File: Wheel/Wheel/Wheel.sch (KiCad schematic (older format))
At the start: 129 parts, among them J1 Conn_02x09_Odd_Even, J10 RJ45, J11 Screw_Terminal_01x02, J12 DS-201, J13 Conn_01x04, J14 Conn_02x13_Top_Bottom, J15 DB25_Female, J16 Conn_01x06, J17 Conn_01x07, J18 Conn_01x06, J19 RJ45, J2 RJ45, J20 DB9_Male, J21 DB9_Female, J22 Conn_02x15_Odd_Even, J3 RJ45, J4 RJ45, J5 USB_B, J6 Conn_02x10_Odd_Even, J7 Conn_02x09_Odd_Even, J8 RJ45, J9 RJ45, U1 MCP23S17_SP, U10 PC817, U11 IP4220CZ6, U12 PC817, U13 IP4220CZ6, U2 STM32F407VETx, U3 MCP23S17_SP, U4 USBLC6-2SC6, U5 AMS1117, U6 4N35, U7 PC817, U8 PC817, U9 PC817, Y1 32,768 кГц, Y2 8MHz

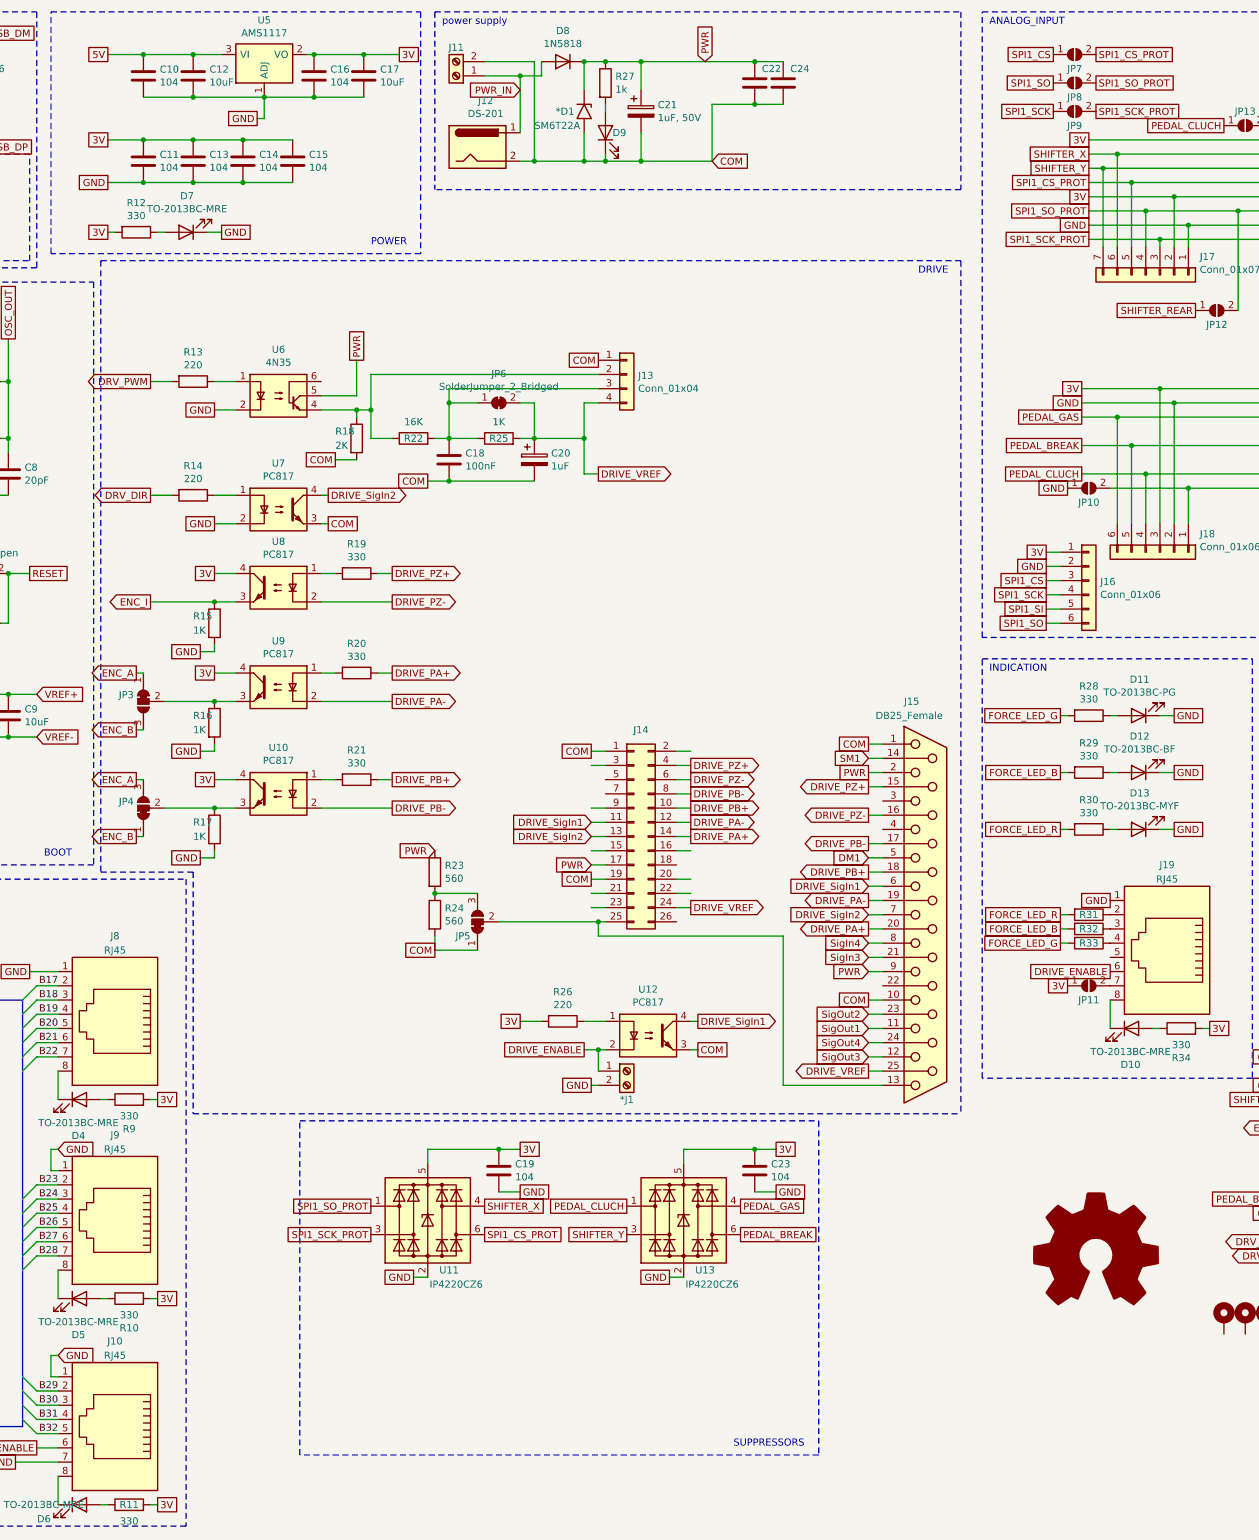
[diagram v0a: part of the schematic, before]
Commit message: I've added supressors for all buttons in the Wheel board
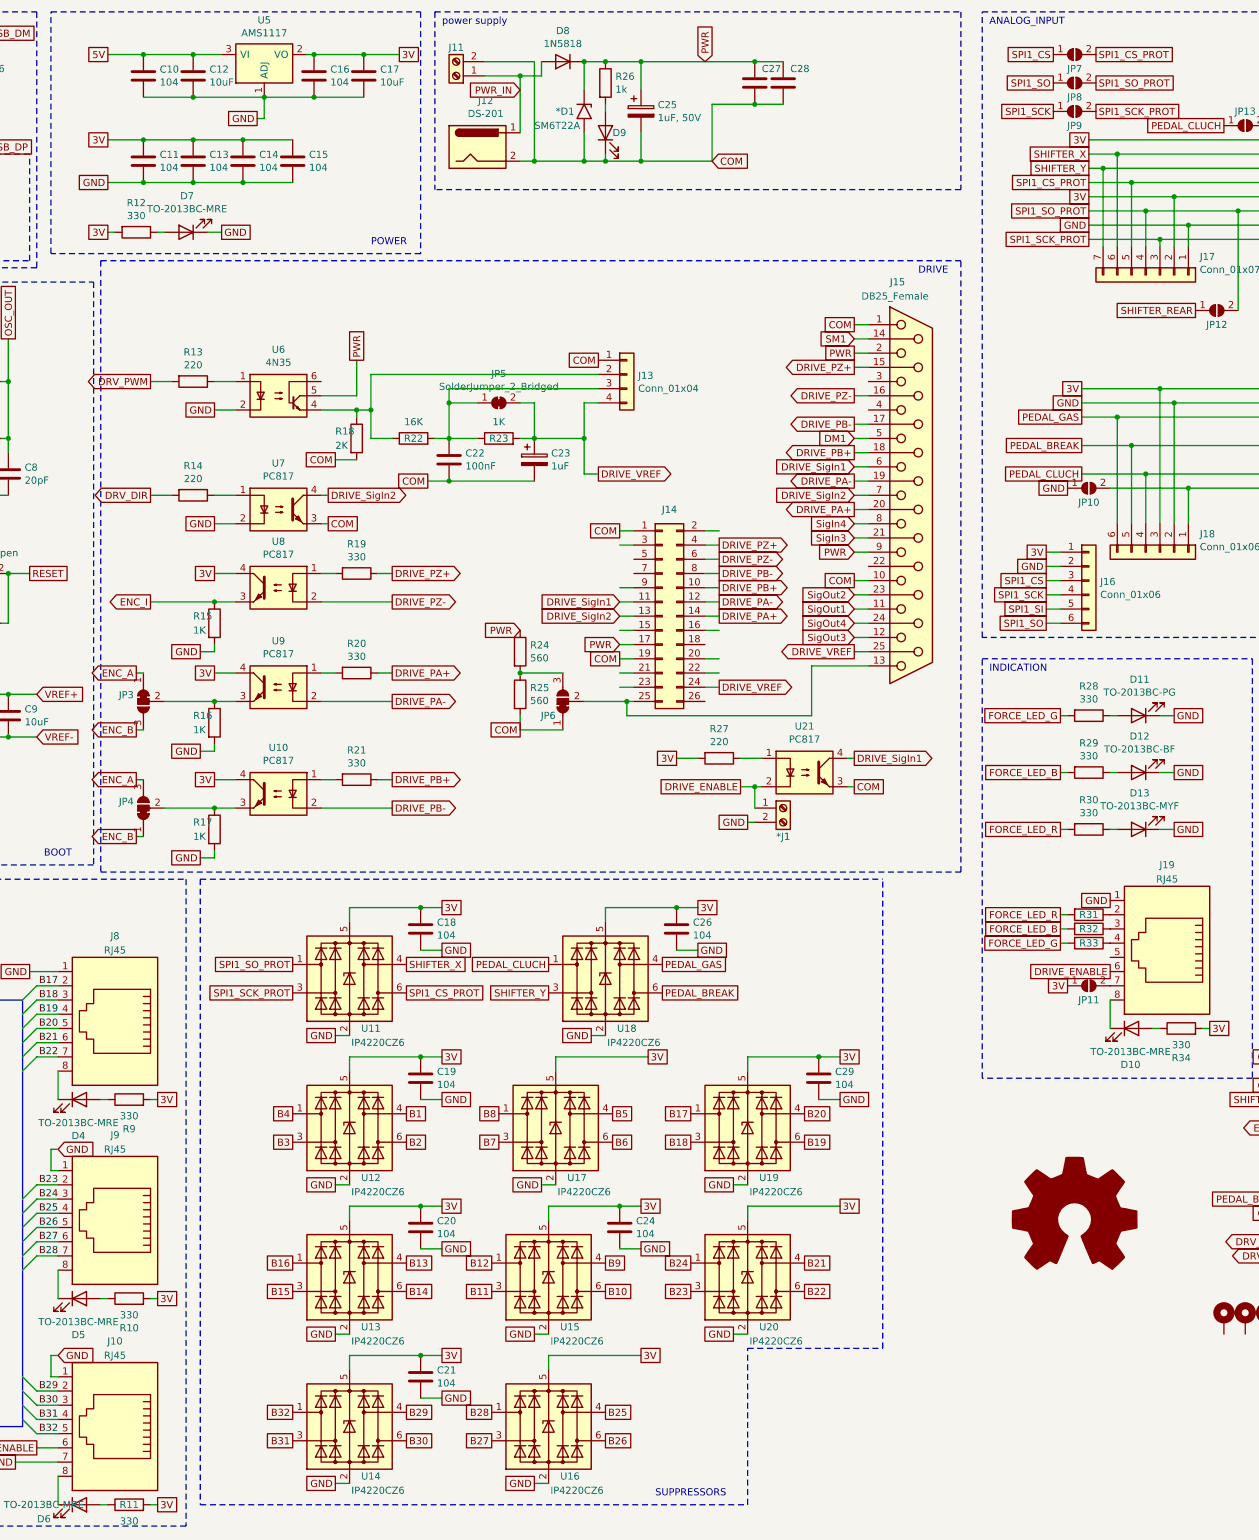
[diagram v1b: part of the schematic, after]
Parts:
- added C19, C20, C21, C24, C29: 104, Capacitor_SMD:C_0805_2012Metric, symbol Device:C
- added U12, U13, U14, U15, U16, U17, U19, U20: IP4220CZ6, Package_SO:TSOP-6_1.65x3.05mm_P0.95mm, symbol Power_Protection:USBLC6-4SC6
- renumbered C19 to C18, C18 to C22, C20 to C23, C21 to C25, C23 to C26, C22 to C27, C24 to C28, JP6 to JP5, JP5 to JP6, R25 to R23, R23 to R24, R24 to R25, R27 to R26, R26 to R27, U13 to U18, U12 to U21
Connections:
- net 3V: now also C19.1, C20.1, C21.1, C24.1, C29.1, U12.5 (VBUS), U13.5 (VBUS), U14.5 (VBUS), U15.5 (VBUS), U16.5 (VBUS), U17.5 (VBUS), U19.5 (VBUS), U20.5 (VBUS)
- net B1: now also U12.4 (I/O3)
- net B10: now also U15.6 (I/O4)
- net B11: now also U15.3 (I/O2)
- net B12: now also U15.1 (I/O1)
- net B13: now also U13.4 (I/O3)
- net B14: now also U13.6 (I/O4)
- net B15: now also U13.3 (I/O2)
- net B16: now also U13.1 (I/O1)
- net B17: now also U19.1 (I/O1)
- net B18: now also U19.3 (I/O2)
- net B19: now also U19.6 (I/O4)
- net B2: now also U12.6 (I/O4)
- net B20: now also U19.4 (I/O3)
- net B21: now also U20.4 (I/O3)
- net B22: now also U20.6 (I/O4)
- net B23: now also U20.3 (I/O2)
- net B24: now also U20.1 (I/O1)
- net B25: now also U16.4 (I/O3)
- net B26: now also U16.6 (I/O4)
- net B27: now also U16.3 (I/O2)
- net B28: now also U16.1 (I/O1)
- net B29: now also U14.4 (I/O3)
- net B3: now also U12.3 (I/O2)
- net B30: now also U14.6 (I/O4)
- net B31: now also U14.3 (I/O2)
- net B4: now also U12.1 (I/O1)
- net B5: now also U17.4 (I/O3)
- net B6: now also U17.6 (I/O4)
- net B7: now also U17.3 (I/O2)
- net B8: now also U17.1 (I/O1)
- net B9: now also U15.4 (I/O3)
- net GND: now also C19.2, C20.2, C21.2, C24.2, C29.2, U12.2 (GND), U13.2 (GND), U14.2 (GND), U15.2 (GND), U16.2 (GND), U17.2 (GND), U19.2 (GND), U20.2 (GND)
- net SHIFTER_REAR renamed B32
- net B32: now also U14.1 (I/O1)
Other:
- moved on the sheet: *J1, C18, C26, J14, J15, JP6, R24, R25, R27, U11, U18, U21

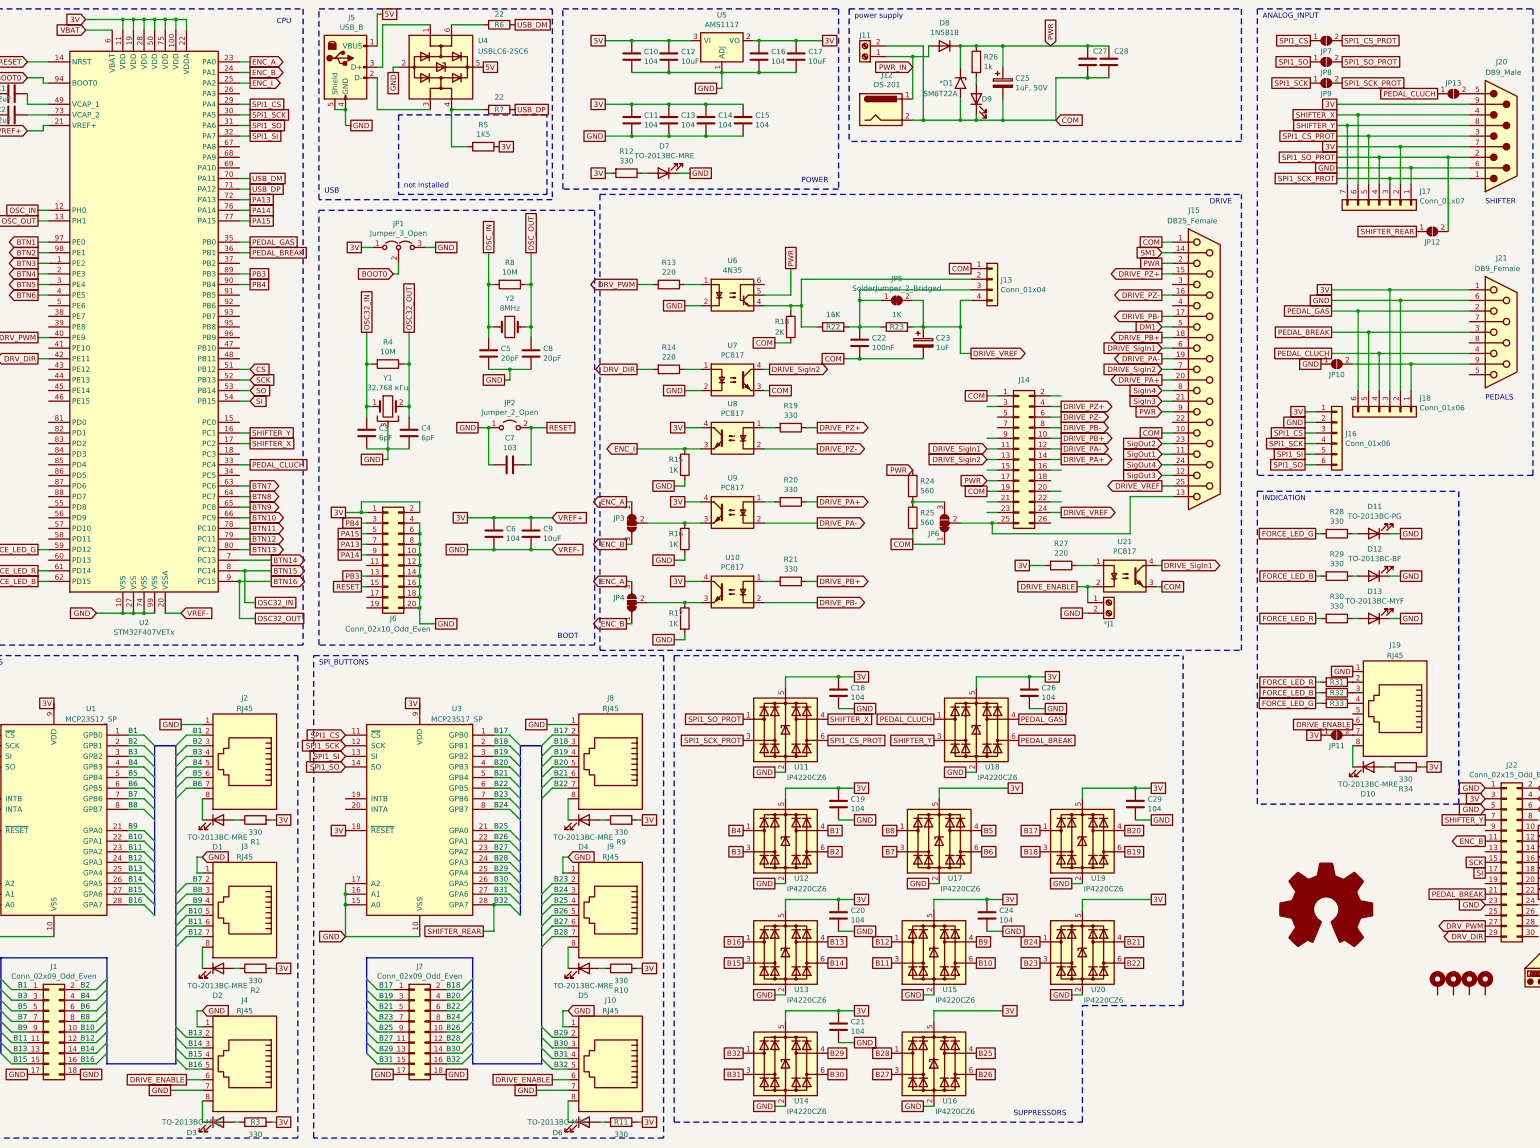
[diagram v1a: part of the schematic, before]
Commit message: I've changed wheel's PCB, I've added GERBER files
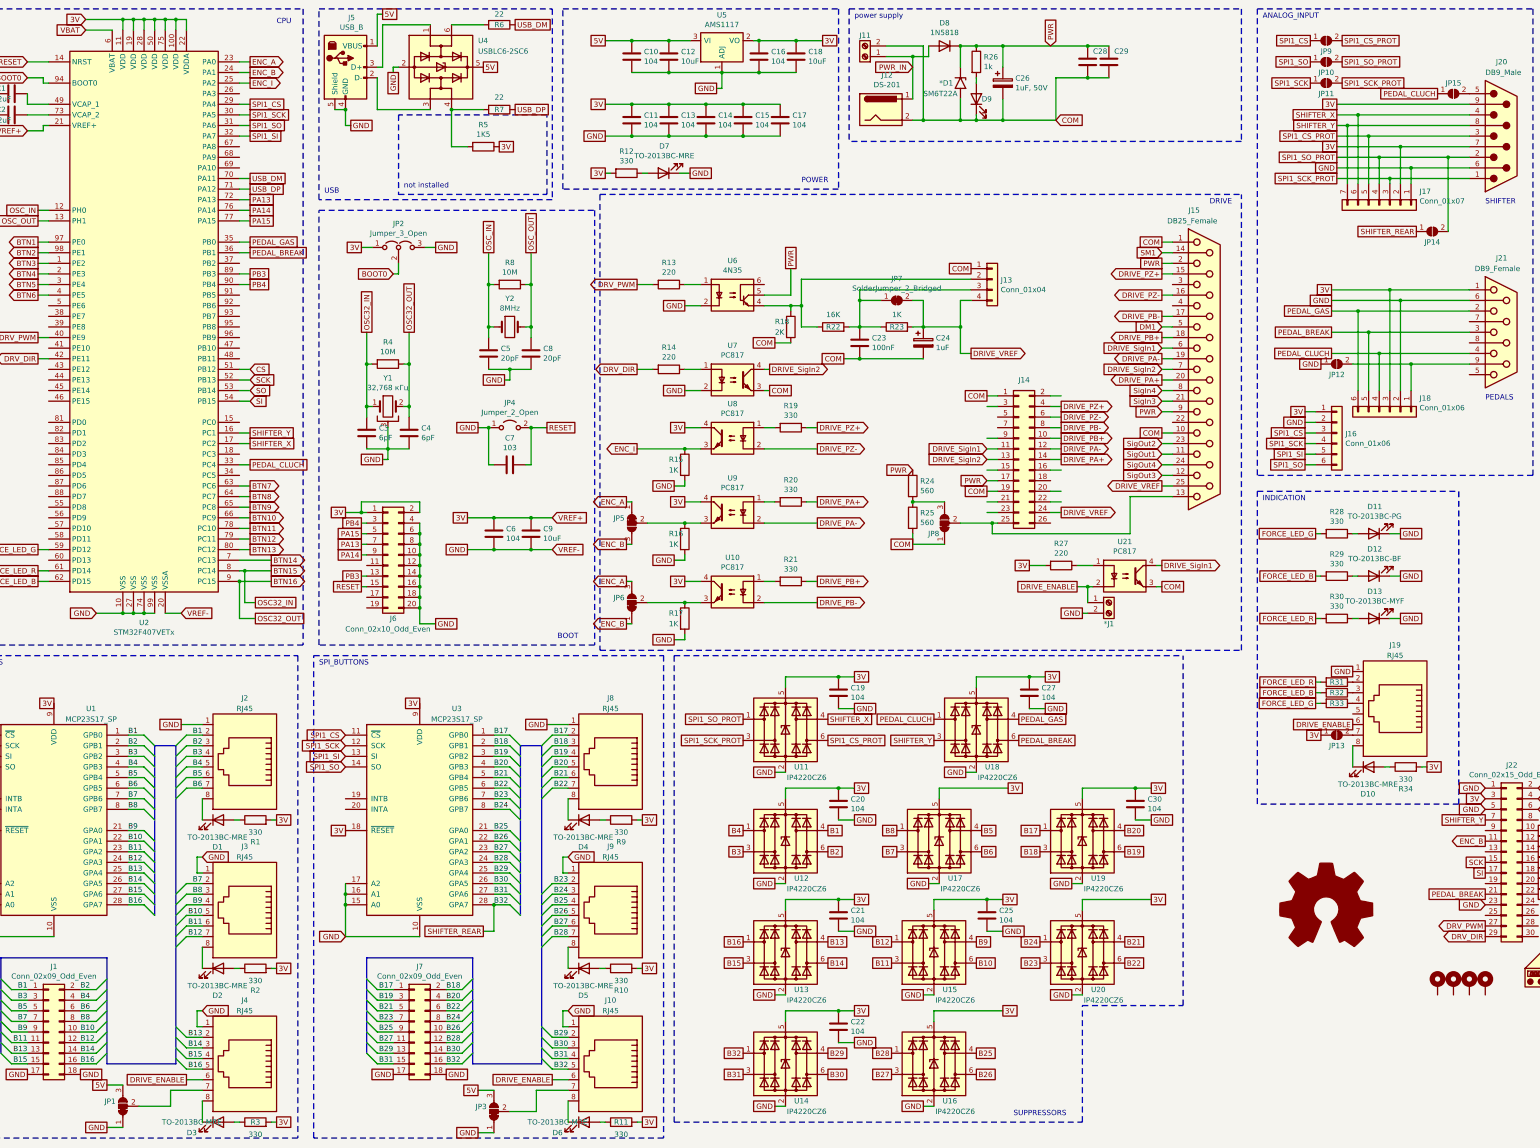
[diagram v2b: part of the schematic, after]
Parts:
- added C17: 104, Capacitor_SMD:C_0805_2012Metric, symbol Device:C
- added JP1, JP3: SolderJumper_3_Bridged12, Jumper:SolderJumper-3_P1.3mm_Bridged12_RoundedPad1.0x1.5mm, symbol Jumper:SolderJumper_3_Bridged12
- renumbered C17 to C18, C18 to C19, C19 to C20, C20 to C21, C21 to C22, C22 to C23, C23 to C24, C24 to C25, C25 to C26, C26 to C27, C27 to C28, C28 to C29, C29 to C30, JP8 to JP10, JP9 to JP11, JP10 to JP12, JP11 to JP13, JP12 to JP14, JP13 to JP15, JP1 to JP2, JP2 to JP4, JP3 to JP5, JP4 to JP6, JP5 to JP7, JP6 to JP8, JP7 to JP9
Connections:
- net 3V: now also C17.1
- net 5V: now also JP1.3 (B), JP3.3 (B)
- net GND: now also C17.2, JP1.1 (A), JP3.1 (A); no longer J10.7, J4.7
- new net: J10.7, JP3.2 (C)
- new net: J4.7, JP1.2 (C)
